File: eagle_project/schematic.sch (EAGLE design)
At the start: 42 parts, among them Q1 BC618, Q2 BC618, U1 MCP4912-E/SL, U10 MCP4912-E/SL, U2 TL084ACN, U3 TL082ACP, U4 MCP1501T-40E/CHY, U5 OP07CD, U6 OP07CD, U7 OP07CD, U9 TL084ACN

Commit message: koncane reference in napajanje
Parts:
- added C10, C7: 1000uF/25V/105°, rcl:CPOL-EUE5-13
- added C11, C15, C8: 1n, rcl:C-EUC0805
- added C12, C3, C9: 100uF, rcl:CPOL-EUE2-5
- added C13, C14, C16, C17, C18, C2, C6: 100nF, rcl:C-EUC0805
- added C4: 470uF/10V/105°C+ FOOTPRINT, rcl:CPOL-EUE3.5-8
- added C5: 100uF/10V/105°, rcl:CPOL-EUE2-5
- added D1, D12, D2: SS13+, diode:SCHOTTKY-DIODESMC
- added IC1, IC2, IC3: AZ34063U, IMPORTED_ELEMENTS:AZ34063U
- added J1: USB-B, IMPORTED:USB-B
- added L1, L3, L5: 100uH, rcl:L-USWE-TPC
- added L2, L4, L6: 1uH, IMPORTED:INDUCTOR
- added LED1, LED2, LED3: (no value), led:LED3MM
- added R29, R30, R35: (no value), rcl:R-EU_R0805
- added R31: 33k, rcl:R-EU_R0805
- added R32: 3k9, rcl:R-EU_R0805
- added R33, R38: 0R24, rcl:R-EU_R0805
- added R34: 75R, rcl:R-EU_R0805
- added R36: 953R, rcl:R-EU_R0805
- added R37: 8k2, rcl:R-EU_R0805
- added R53: 3k3, rcl:R-EU_R0805
- added R54: 2k, rcl:R-EU_R0805
- added R63: 1R5, rcl:R-EU_R0805
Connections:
- removed net 12V: U2.VCC+, U3.VCC+, U9.VCC+
- new net +12V: C9.+, L4.2, R30.2, U2.VCC+, U3.VCC+, U9.VCC+
- new net +3V3: C3.+, L2.2, R29.2
- new net +5V: C5.+, L1.2, L2.1, R53.2
- new net +5V1: C7.+, D1.C, L4.1, R31.2
- new net +5V2: C10.-, C11.2, D2.A, IC2.GND, L6.1, R36.2
- new net D+: J1.3
- new net D-: J1.2
- new net N$15: LED1.A, R29.1
- new net N$16: LED2.A, R30.1
- new net N$17: IC1.COMP_INV_IN, R31.1, R32.2
- new net N$18: IC1.IPK_SENSE, L3.1, R33.2, R34.1
- new net N$19: LED3.C, R35.1
- new net N$21: C8.1, IC1.TC
- new net N$29: IC1.DRVC, R34.2
- new net N$30: D1.A, IC1.SWC, L3.2
- new net N$31: IC2.COMP_INV_IN, R36.1, R37.2
- new net N$33: IC2.DRVC, IC2.IPK_SENSE, IC2.SWC, R38.2
- new net N$34: C11.1, IC2.TC
- new net N$42: D2.C, IC2.SWE, L5.1
- new net N$69: C15.1, IC3.TC
- new net N$70: IC3.COMP_INV_IN, R53.1, R54.2
- new net N$82: IC3.DRVC, IC3.IPK_SENSE, IC3.SWC, R63.2
- new net N$83: D12.C, IC3.SWE, L1.1
- new net VDD1: C13.1
- net -12V: now also C12.-, L6.2, R35.2
- net GND: now also C10.+, C12.+, C13.2, C14.1, C15.2, C16.1, C17.1, C18.1, C2.2, C3.-, C4.-, C5.-, C6.2, C7.-, C8.2, C9.-, D12.A, IC1.GND, IC1.SWE, IC3.GND, J1.4, L5.2, LED1.C, LED2.C, LED3.A, R32.1, R37.1, R54.1
- net VDD: now also C14.2, C16.2, C17.2, C18.2, C2.1, C4.+, C6.1, IC1.VCC, IC2.VCC, IC3.VCC, J1.1, R33.1, R38.1, R63.1
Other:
- note added: "OPCIJSKO"
- note removed: "OPCIJSKO določi še package"

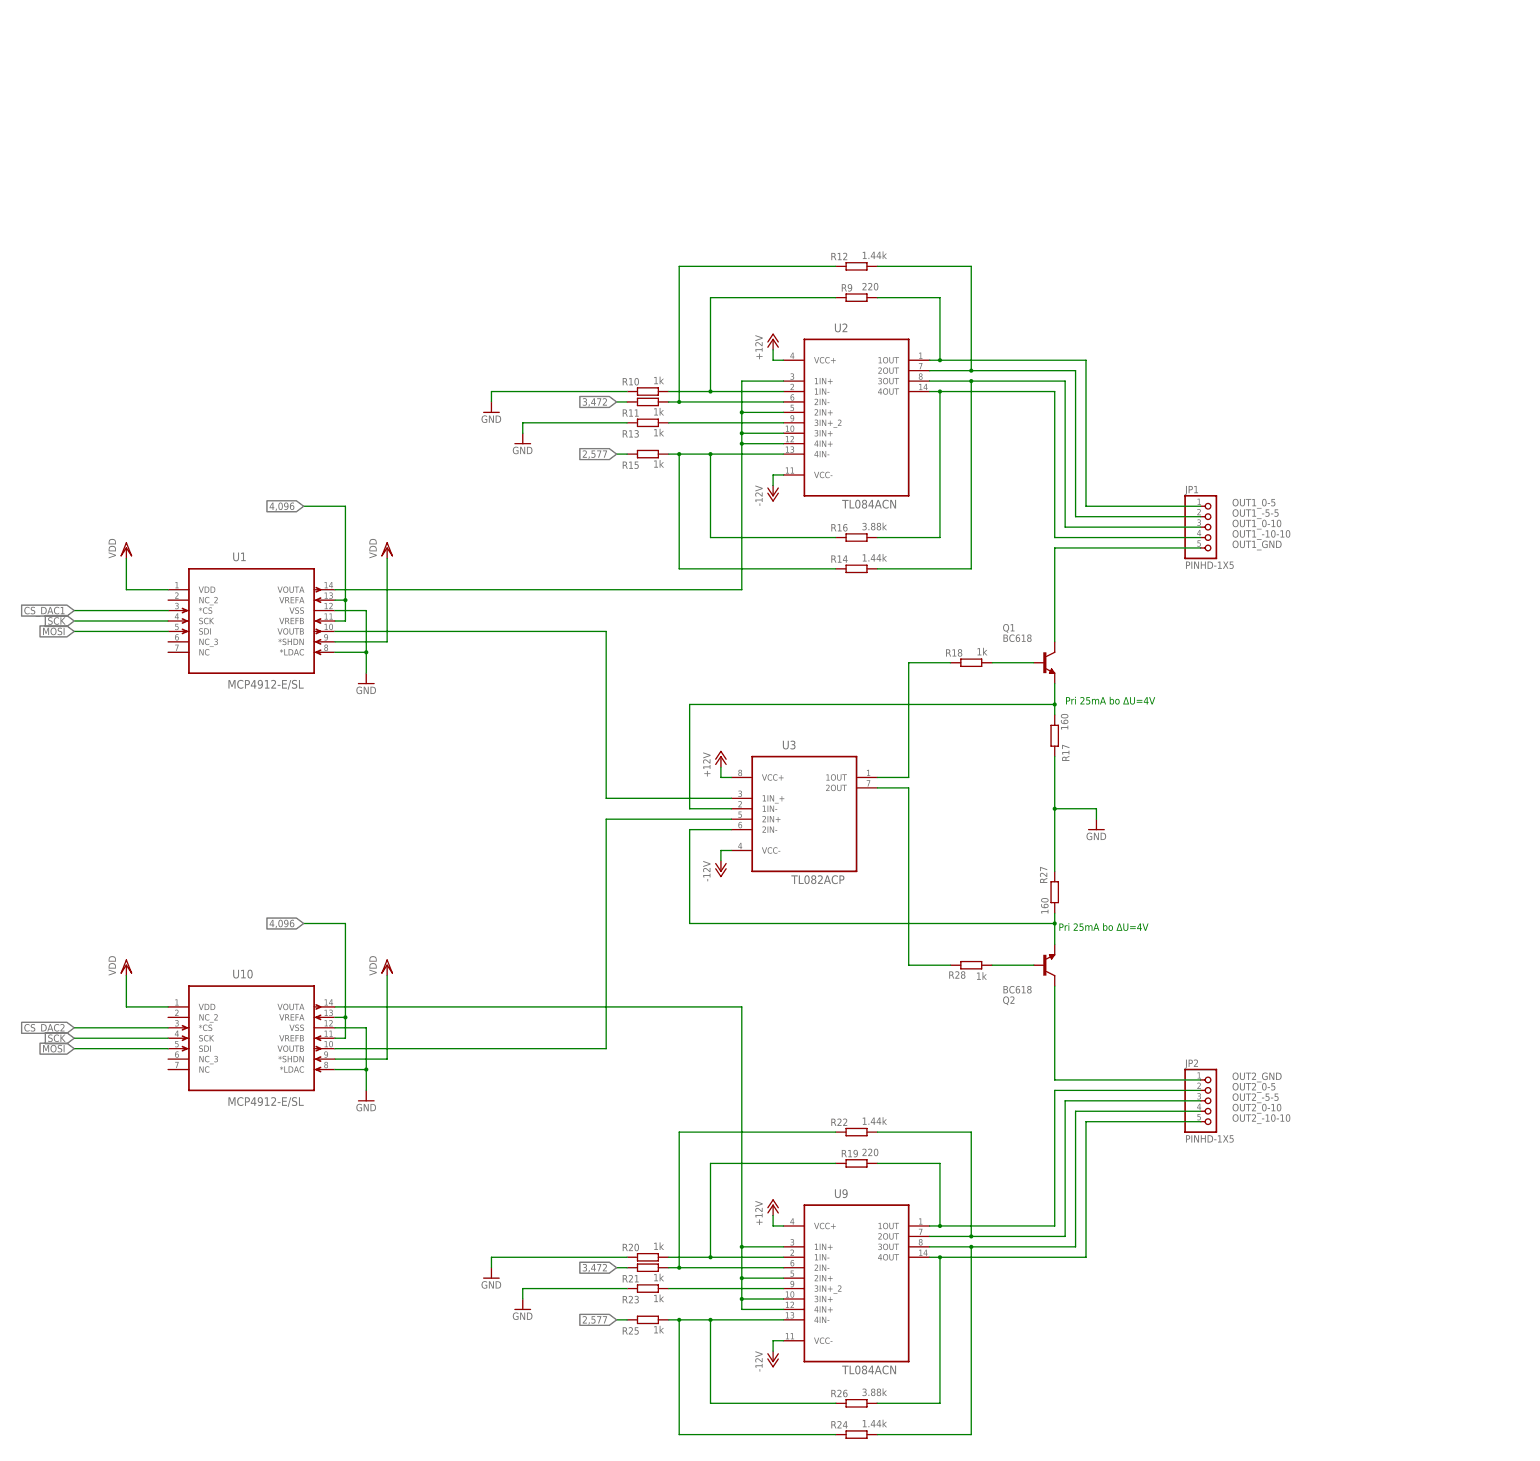
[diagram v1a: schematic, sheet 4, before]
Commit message: Updated analog outputs. Removed op amps and added secector switches
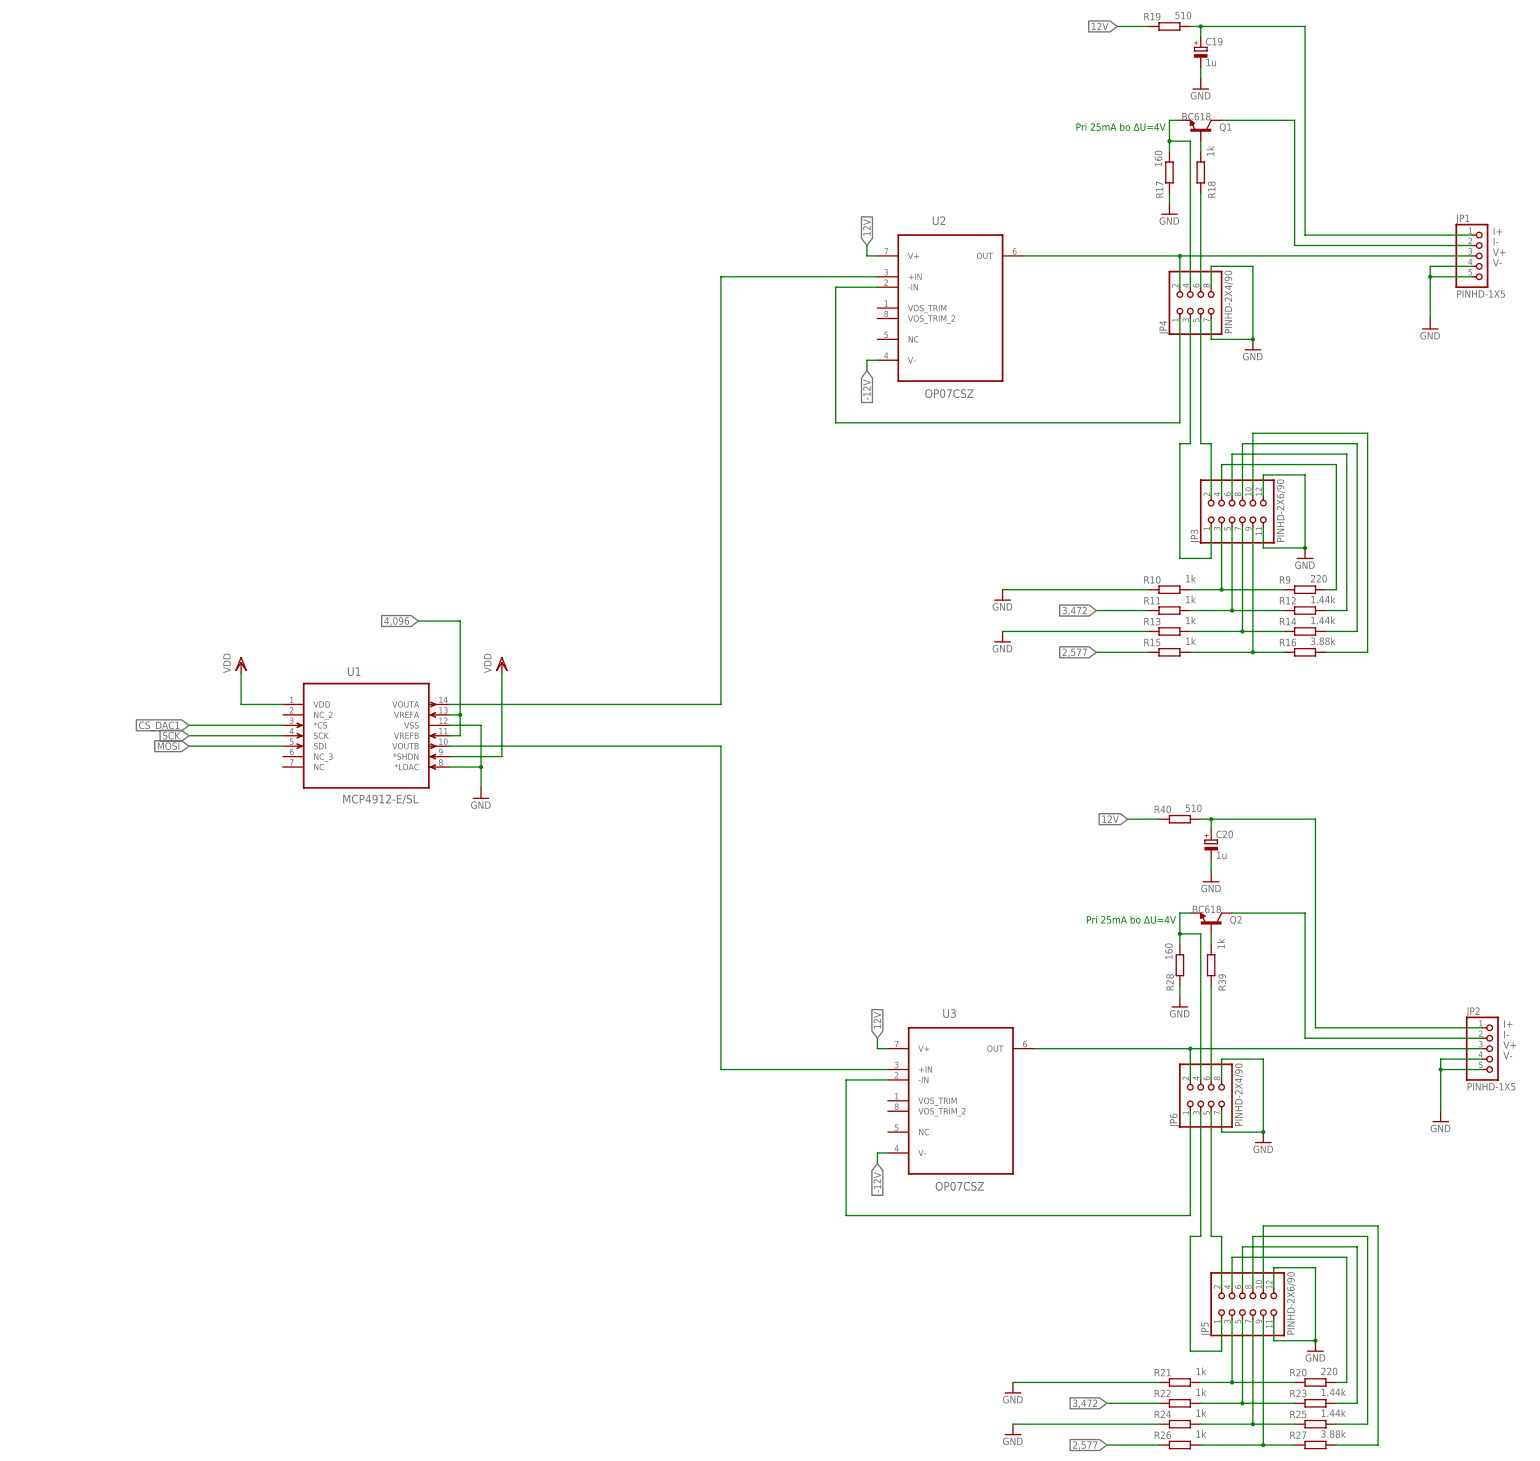
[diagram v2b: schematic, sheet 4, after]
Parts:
- removed U10: MCP4912-E/SL, Microchip_By_element14_Batch_1:MCP4912-E/SL
- removed U9: TL084ACN, Texas Instruments_By_element14_Batch_1:TL084ACN
- added C19, C20: 1u, resistor:CPOL-EUE2-5
- added JP3, JP5: PINHD-2X6/90, Connector:PINHD-2X6/90
- added JP4, JP6: PINHD-2X4/90, Connector:PINHD-2X4/90
- added R39: 1k, resistor:R-EU_0207/7
- added R40: 510, resistor:R-EU_0207/7
- R19: value 220 -> 510
- R20: value 1k -> 220
- R22, R24: value 1.44k -> 1k
- R23, R25: value 1k -> 1.44k
- R26: value 3.88k -> 1k
- R27: value 160 -> 3.88k
- R28: value 1k -> 160
- U2: value TL084ACN -> OP07CSZ; device Texas Instruments_By_element14_Batch_1:TL084ACN -> Analog Devices_By_element14_Batch_1:OP07CSZ
- U3: value TL082ACP -> OP07CSZ; device Texas Instruments_By_element14_Batch_1:TL082ACP -> Analog Devices_By_element14_Batch_1:OP07CSZ
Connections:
- removed net CS_DAC2: U10.*CS
- removed net OUT1_-10-10: JP1.4, R16.2, U2.4OUT
- removed net OUT1_-5-5: JP1.2, R12.2, U2.2OUT
- removed net OUT1_0-10: JP1.3, R14.2, U2.3OUT
- removed net OUT1_0-5: JP1.1, R9.2, U2.1OUT
- removed net OUT1_GND: JP1.5, Q1.C
- removed net OUT2_-10-10: JP2.5, R26.2, U9.4OUT
- removed net OUT2_-5-5: JP2.3, R22.2, U9.2OUT
- removed net OUT2_0-10: JP2.4, R24.2, U9.3OUT
- removed net OUT2_0-5: JP2.2, R19.2, U9.1OUT
- removed net OUT2_GND: JP2.1, Q2.C
- new net 12V: R19.1, R40.1, U2.V+, U3.V+
- new net I+: C19.+, C20.+, JP1.1, JP2.1, R19.2, R40.2
- new net I-: JP1.2, JP2.2, Q1.C, Q2.C
- new net N$40: JP4.6, R18.1
- new net N$41: JP5.7, R24.2, R25.1
- new net N$43: JP5.9, R26.2, R27.1
- new net N$44: JP5.5, R22.2, R23.1
- new net N$45: JP5.4, R20.2
- new net N$46: JP5.6, R23.2
- new net N$47: JP5.8, R25.2
- new net N$48: JP5.10, R27.2
- new net N$49: JP6.1, U3.-IN
- new net N$50: JP5.1, JP6.3
- new net N$51: JP5.2, JP6.5
- new net N$52: JP6.6, R39.1
- new net V+: JP1.3, JP2.3, JP4.2, JP6.2, U2.OUT, U3.OUT
- new net V-: JP1.4, JP1.5, JP2.4, JP2.5
- net +12V: no longer U2.VCC+, U3.VCC+, U9.VCC+
- net -12V: now also U2.V-, U3.V-; no longer U2.VCC-, U3.VCC-, U9.VCC-
- net 2,577: now also R26.1; no longer R25.1
- net 3,472: now also R22.1; no longer R21.1
- net 4,096: no longer U10.VREFA, U10.VREFB
- net GND: now also C19.-, C20.-, JP3.11, JP3.12, JP4.7, JP4.8, JP5.11, JP5.12, JP6.7, JP6.8, R21.1, R24.1, R28.1; no longer R20.1, R23.1, R27.1, U10.*LDAC, U10.VSS
- net MOSI: no longer U10.SDI
- net N$11: now also JP3.3; no longer U2.1IN-
- net N$12: now also JP3.7, R13.2, R14.1; no longer R11.2, R12.1, U2.2IN-
- net N$13: now also JP3.9, R15.2, R16.1; no longer R13.2, U2.3IN+_2
- net N$14: now also JP3.5, R11.2, R12.1; no longer R14.1, R15.2, R16.1, U2.4IN-
- net N$20: now also U2.+IN; no longer U2.1IN+, U2.2IN+, U2.3IN+, U2.4IN+
- net N$23: now also JP3.4, R9.2; no longer R19.1, R20.2, U9.1IN-
- net N$24: now also U3.+IN; no longer U3.1IN_+
- net N$25: now also JP4.4; no longer U3.1IN-
- net N$26: now also JP3.6, R12.2; no longer R21.2, R22.1, U9.2IN-
- net N$27: now also JP3.8, R14.2; no longer R23.2, U9.3IN+_2
- net N$28: now also JP3.10, R16.2; no longer R24.1, R25.2, R26.1, U9.4IN-
- net N$32: now also JP4.1, U2.-IN; no longer U10.VOUTA, U9.1IN+, U9.2IN+, U9.3IN+, U9.4IN+
- net N$35: now also JP3.1, JP4.3; no longer Q2.B, R28.1
- net N$36: now also JP3.2, JP4.5; no longer R18.1, U3.1OUT
- net N$37: now also Q2.B, R39.2; no longer Q2.E, R27.2, U3.2IN-
- net N$38: now also JP6.4, Q2.E; no longer U3.2OUT
- net N$39: now also JP5.3, R20.1, R21.2; no longer U10.VOUTB, U3.2IN+
- net SCK: no longer U10.SCK
- net VDD: no longer U10.*SHDN, U10.VDD
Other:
- moved on the sheet: JP1, JP2, Q1, Q2, R10, R11, R12, R13, R14, R15, R16, R17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

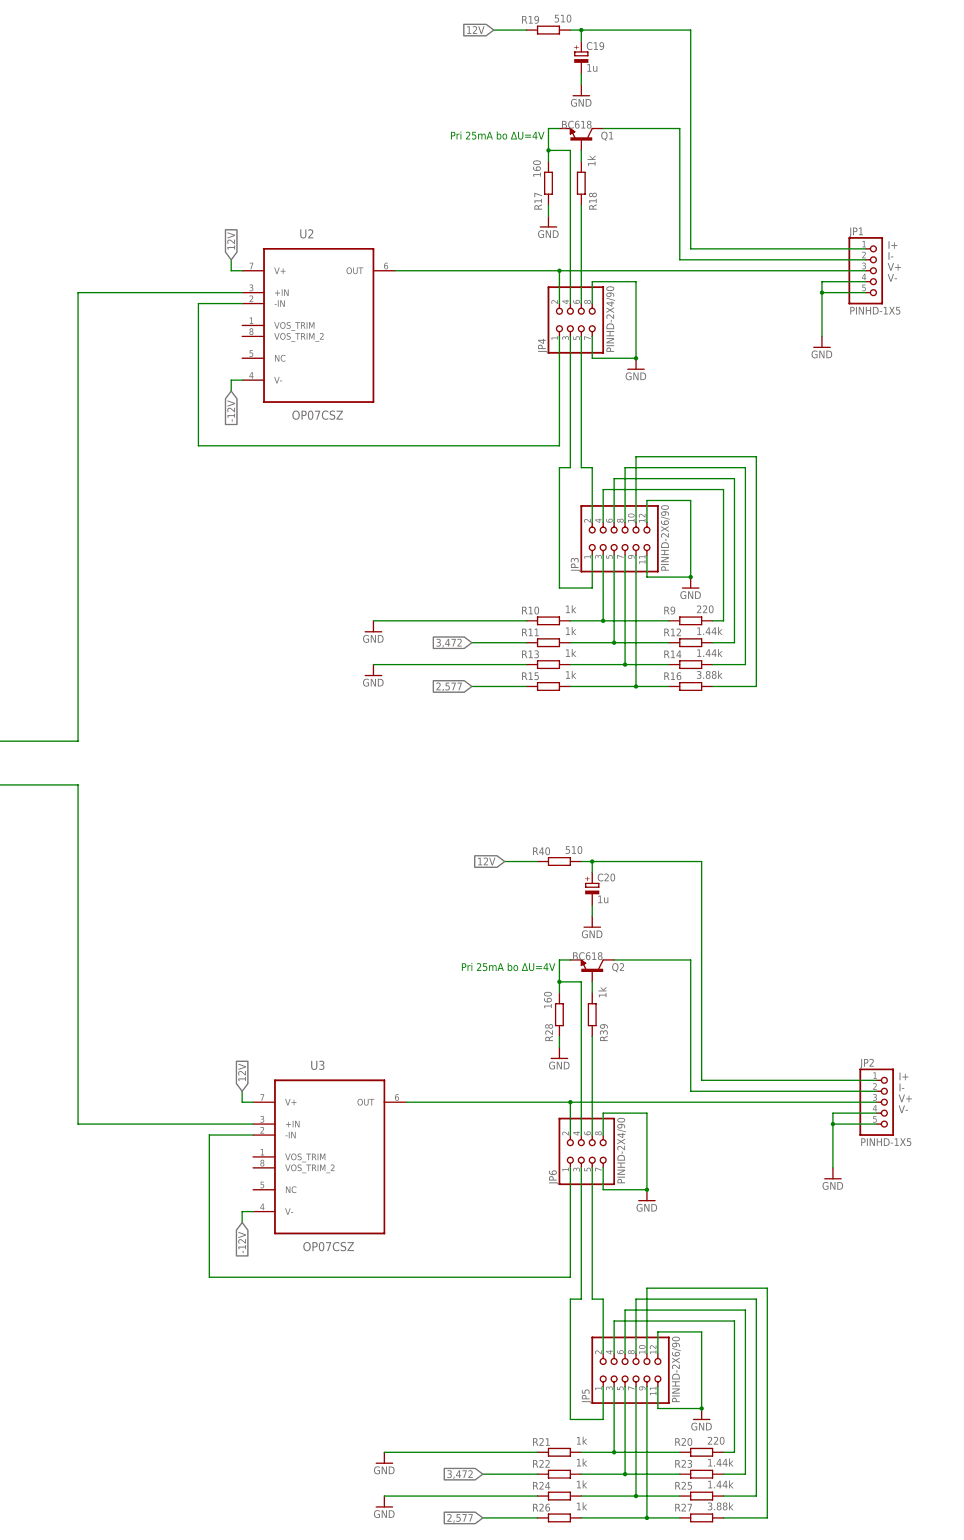
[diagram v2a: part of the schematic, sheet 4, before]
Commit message: Analog outputs: added trimmers and fixed voltage labels
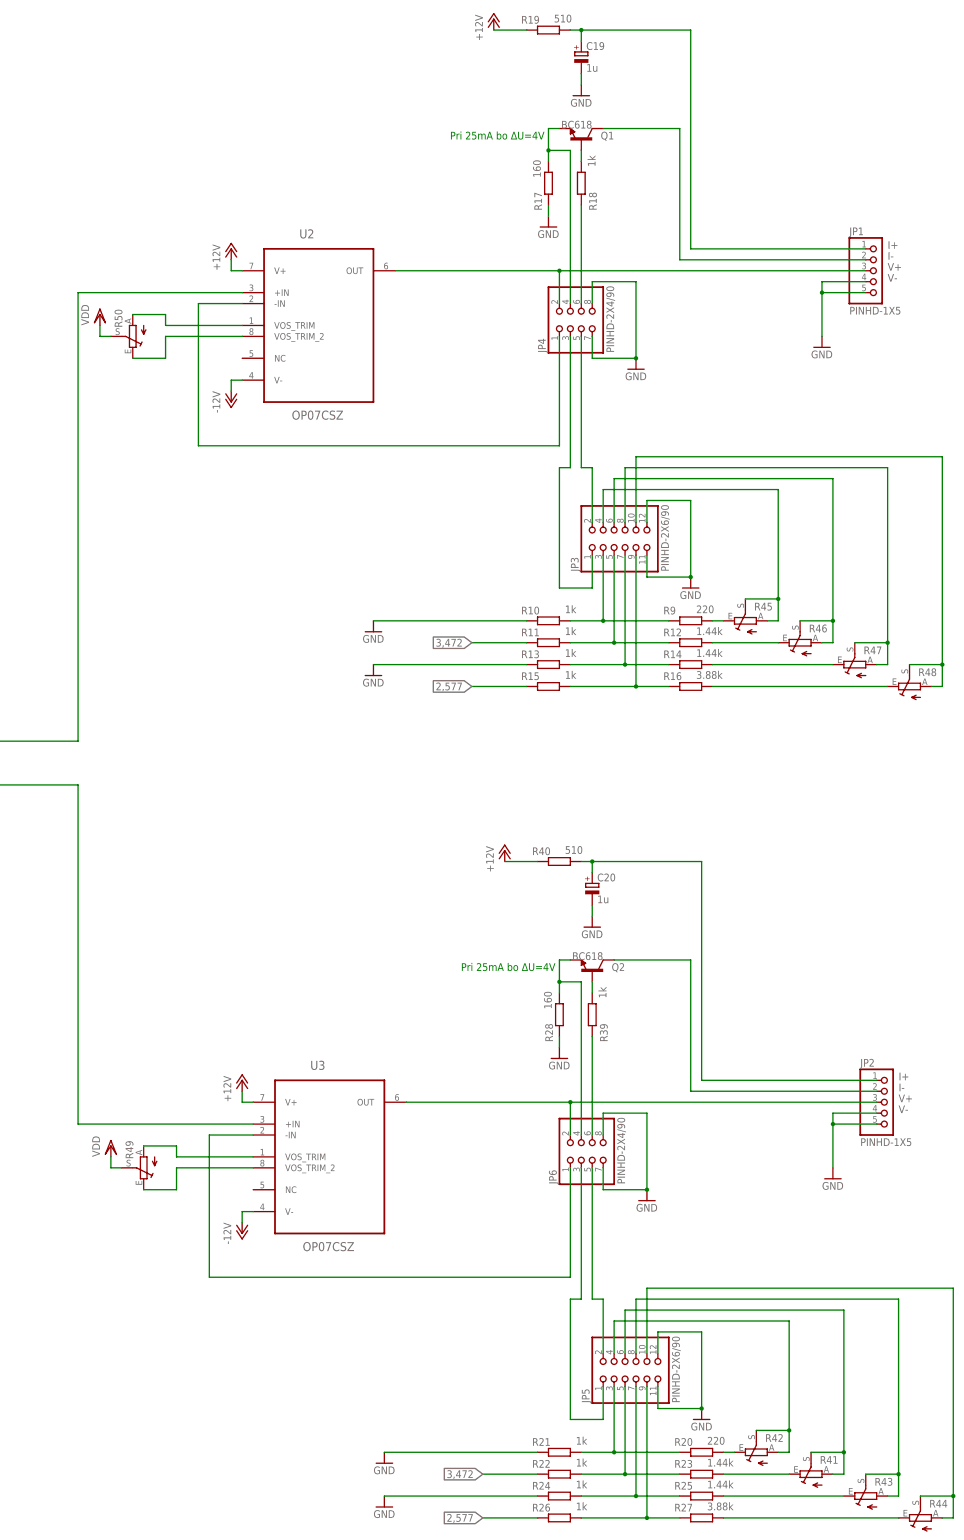
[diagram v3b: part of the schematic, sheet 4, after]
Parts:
- added R41, R42, R43, R44, R45, R46, R47, R48, R49, R50: (no value), pot:TRIM_EU-S64W
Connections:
- removed net 12V: R19.1, R40.1, U2.V+, U3.V+
- new net N$53: R20.2, R42.E
- new net N$54: JP5.6, R41.A, R41.S
- new net N$55: JP5.4, R42.A, R42.S
- new net N$56: R25.2, R43.E
- new net N$57: JP5.10, R44.A, R44.S
- new net N$58: R27.2, R44.E
- new net N$59: R49.E, U3.VOS_TRIM_2
- new net N$60: R50.A, U2.VOS_TRIM
- new net N$61: R50.E, U2.VOS_TRIM_2
- new net N$62: R12.2, R46.E
- new net N$63: R14.2, R47.E
- new net N$64: R16.2, R48.E
- net +12V: now also R19.1, R40.1, U2.V+, U3.V+
- net N$23: now also R45.A, R45.S; no longer R9.2
- net N$26: now also R46.A, R46.S; no longer R12.2
- net N$27: now also R47.A, R47.S; no longer R14.2
- net N$28: now also R48.A, R48.S; no longer R16.2
- net N$45: now also JP5.8, R43.A, R43.S; no longer JP5.4, R20.2
- net N$46: now also R41.E; no longer JP5.6
- net N$47: now also R45.E, R9.2; no longer JP5.8, R25.2
- net N$48: now also R49.A, U3.VOS_TRIM; no longer JP5.10, R27.2
- net VDD: now also R49.S, R50.S
